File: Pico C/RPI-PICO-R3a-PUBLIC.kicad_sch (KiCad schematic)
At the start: 37 parts, among them IC1 W25Q16JVUXIQ, J1 CON_PICO_40W_VER_C, J2 USB_C_Receptacle_USB2.0_16P, J3 SM03B-SRSS-TB, Q1 DMG1012T-7, U2 RT6150B-33GQW, Y1 ECS-120-8-33-JGN-TR

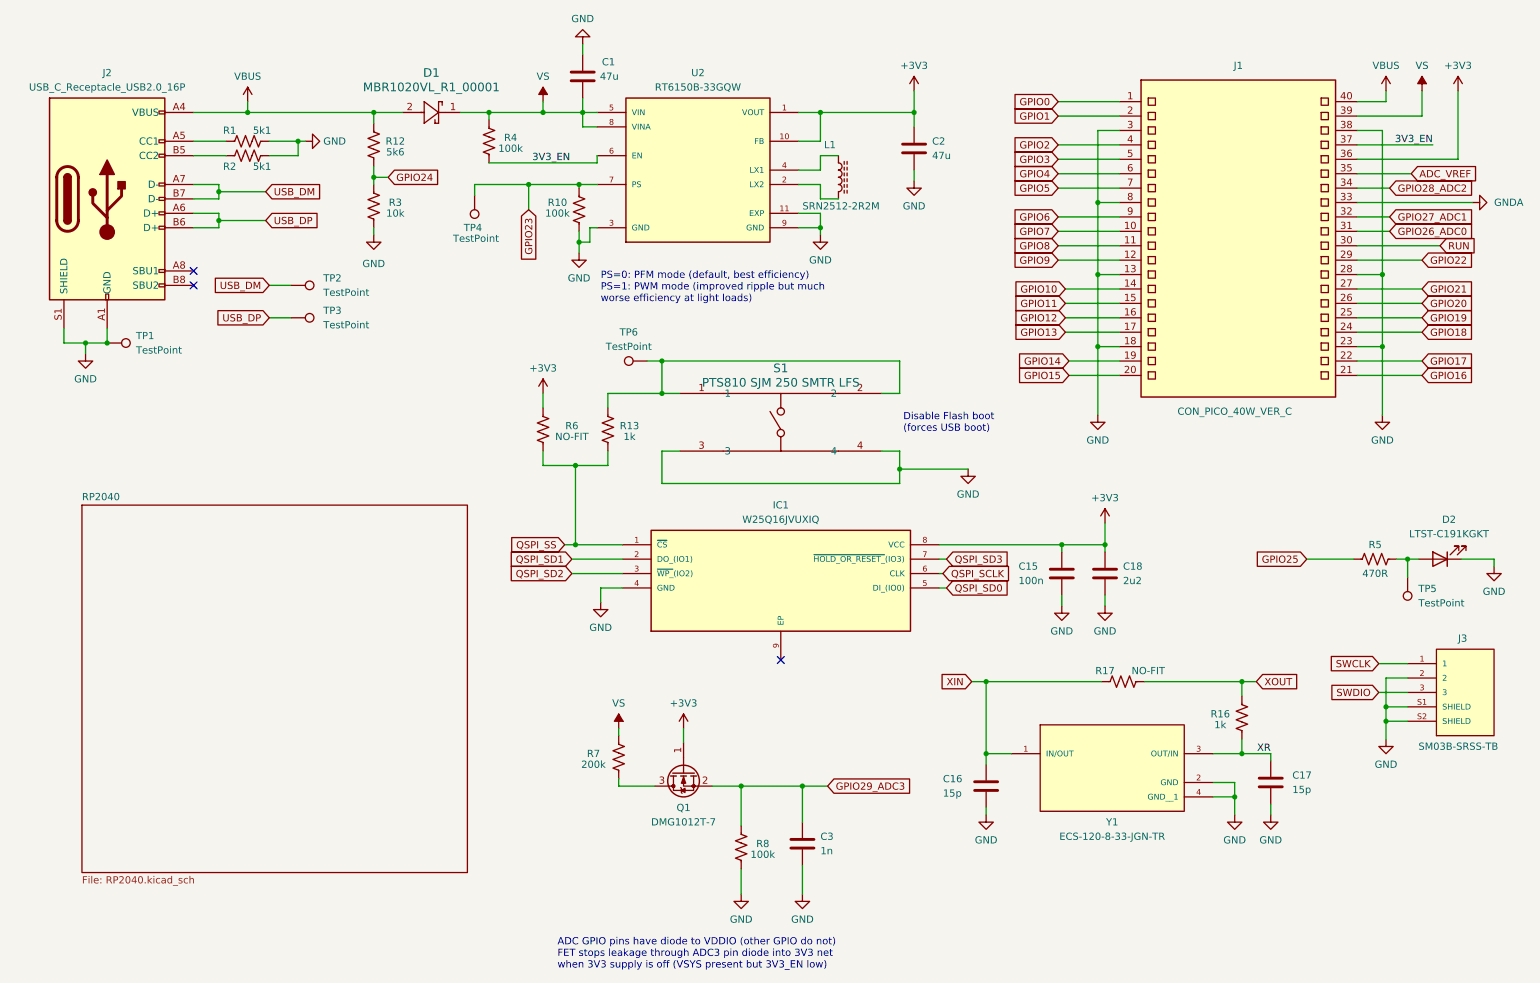
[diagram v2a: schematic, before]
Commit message: Add files via upload
Updated design and included official design file from the Pi Foundation.
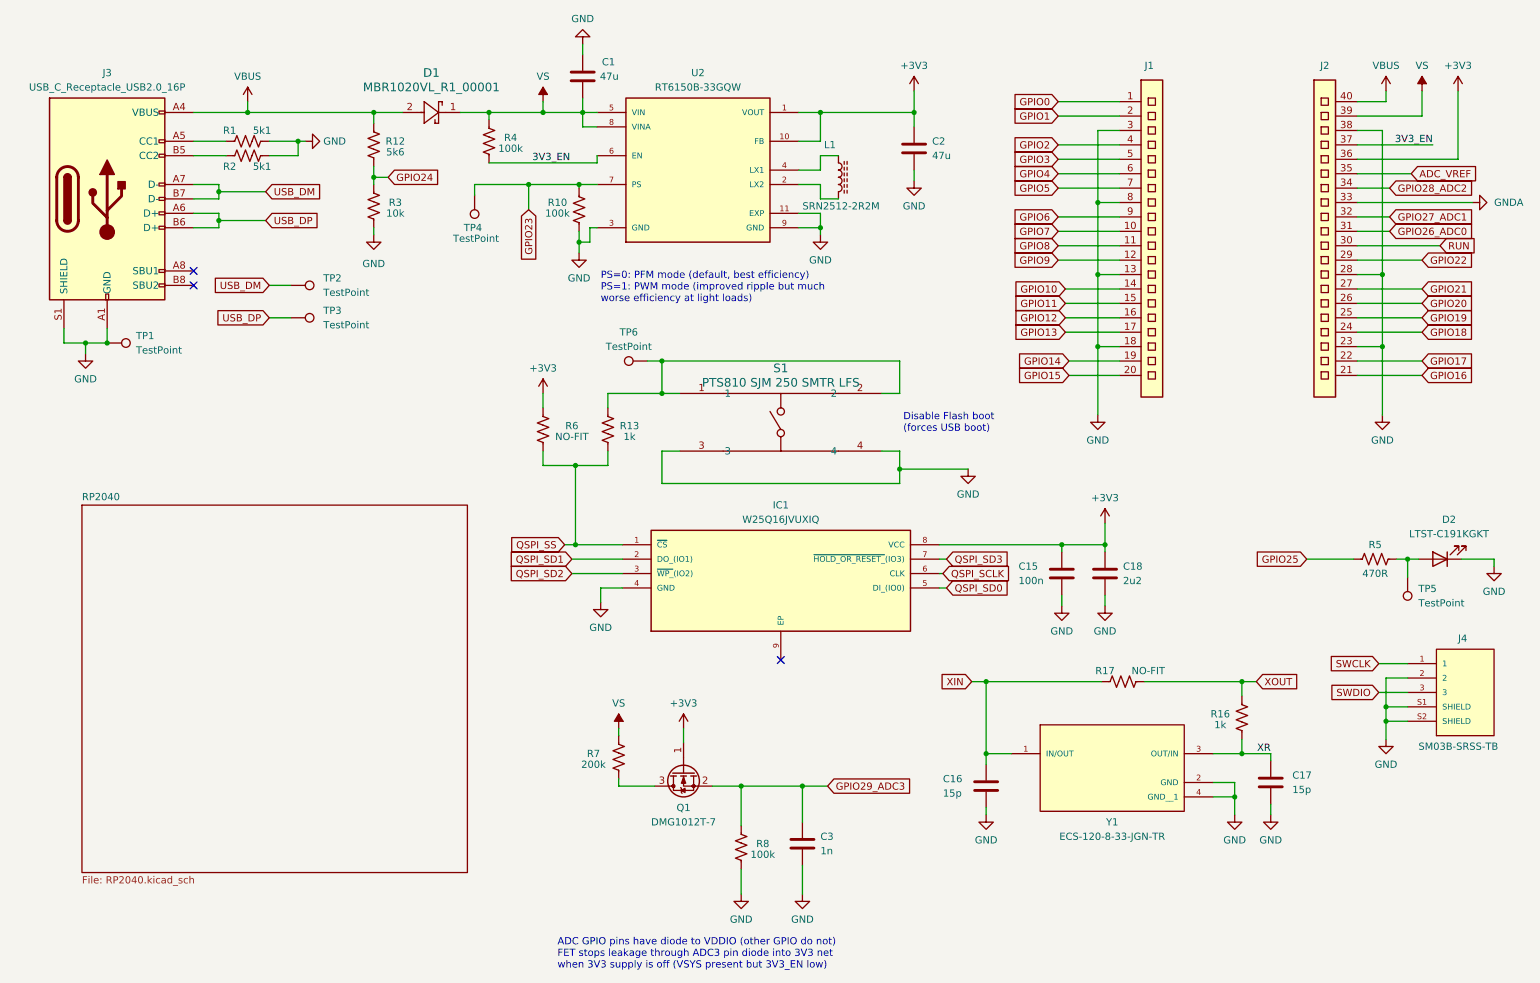
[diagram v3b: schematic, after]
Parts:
- removed J1: CON_PICO_40W_VER_C, Pico_C:CON_PICO_40W_VER_C, symbol Pico_C:CON_PICO_40W_VER_C
- removed J2: USB_C_Receptacle_USB2.0_16P, Connector_USB:USB_C_Receptacle_GCT_USB4105-xx-A_16P_TopMnt_Horizontal, symbol Connector:USB_C_Receptacle_USB2.0_16P
- removed J3: SM03B-SRSS-TB, Pico_C:JST_SM03B-SRSS-TB_LF__SN_, symbol Pico_C:SM03B-SRSS-TB_LF__SN_
- added J1: ~, Pico_C:CON_PICO_1-20, symbol Pico_C:CON_PICO_1-20
- added J2: ~, Pico_C:CON_PICO_21-40, symbol Pico_C:CON_PICO_21-40
- added J3: USB_C_Receptacle_USB2.0_16P, Connector_USB:USB_C_Receptacle_GCT_USB4105-xx-A_16P_TopMnt_Horizontal, symbol Connector:USB_C_Receptacle_USB2.0_16P
- added J4: SM03B-SRSS-TB, Pico_C:JST_SM03B-SRSS-TB_LF__SN_, symbol Pico_C:SM03B-SRSS-TB_LF__SN_
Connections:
- net +3V3: now also J2.36
- net 3V3_EN: now also J2.37
- net ADC_VREF: now also J2.35
- net GND: now also J1.13, J1.18, J1.3, J1.8, J2.23, J2.28, J2.38, J3.A1 (GND), J3.A12 (GND), J3.B1 (GND), J3.B12 (GND), J3.S1 (SHIELD), J4.2, J4.S1 (SHIELD), J4.S2 (SHIELD)
- net GNDA: now also J2.33
- net GPIO0: now also J1.1
- net GPIO1: now also J1.2
- net GPIO10: now also J1.14
- net GPIO11: now also J1.15
- net GPIO12: now also J1.16
- net GPIO13: now also J1.17
- net GPIO14: now also J1.19
- net GPIO15: now also J1.20
- net GPIO16: now also J2.21
- net GPIO17: now also J2.22
- net GPIO18: now also J2.24
- net GPIO19: now also J2.25
- net GPIO2: now also J1.4
- net GPIO20: now also J2.26
- net GPIO21: now also J2.27
- net GPIO22: now also J2.29
- net GPIO26_ADC0: now also J2.31
- net GPIO27_ADC1: now also J2.32
- net GPIO28_ADC2: now also J2.34
- net GPIO3: now also J1.5
- net GPIO4: now also J1.6
- net GPIO5: now also J1.7
- net GPIO6: now also J1.9
- net GPIO7: now also J1.10
- net GPIO8: now also J1.11
- net GPIO9: now also J1.12
- net RUN: now also J2.30
- net SWCLK: now also J4.1
- net SWDIO: now also J4.3
- net USB_DM: now also J3.A7 (D-), J3.B7 (D-)
- net USB_DP: now also J3.A6 (D+), J3.B6 (D+)
- net VBUS: now also J2.40, J3.A4 (VBUS), J3.A9 (VBUS), J3.B4 (VBUS), J3.B9 (VBUS)
- net VS: now also J2.39
- net at R1.1: now also J3.A5 (CC1)
- net at R2.1: now also J3.B5 (CC2)
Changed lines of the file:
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@@
-    )
-  )
-  (symbol (lib_id "Pico_C:SM03B-SRSS-TB_LF__SN_") (at 269.875 135.89 0) (unit 1)
-    (in_bom yes) (on_board yes) (dnp no)
-    (property "Reference" "J3" (at 268.605 126.365 0)
-      (effects (font (size 1.27 1.27)) (justify left))
-    )
-    (property "Value" "SM03B-SRSS-TB" (at 261.62 145.415 0)
-      (effects (font (size 1.27 1.27)) (justify left))
-    )
-    (property "Footprint" "Pico_C:JST_SM03B-SRSS-TB_LF__SN_" (at 269.875 135.89 0)
-      (effects (font (size 1.27 1.27)) (justify bottom) hide)
-    )
-    (property "Datasheet" "https://www.jst-mfg.com/product/pdf/eng/eSH.pdf" (at 269.875 135.89 0)
-      (effects (font (size 1.27 1.27)) hide)
-    )
-    (pin "2")
-    (pin "3")
-    (pin "S2")
-    (pin "1")
-    (pin "S1")
-    (instances
-      (project "RPI-PICO-R3a-PUBLIC"
-        (path "/f8a1033e-7d4e-4018-9b4c-1da5b150b31c"
-          (reference "J3") (unit 1)
-        )
-      )
     )
   )
@@
     )
   )
+  (symbol (lib_id "Connector:USB_C_Receptacle_USB2.0_16P") (at 30.48 48.895 0) (unit 1)
+    (in_bom yes) (on_board yes) (dnp no)
+    (property "Reference" "J3" (at 30.48 26.67 0)
+      (effects (font (size 1.27 1.27)))
+    )
+    (property "Value" "USB_C_Receptacle_USB2.0_16P" (at 30.48 29.21 0)
+      (effects (font (size 1.27 1.27)))
+    )
+    (property "Footprint" "Connector_USB:USB_C_Receptacle_GCT_USB4105-xx-A_16P_TopMnt_Horizontal" (at 34.29 48.895 0)
+      (effects (font (size 1.27 1.27)) hide)
+    )
+    (property "Datasheet" "https://www.usb.org/sites/default/files/documents/usb_type-c.zip" (at 34.29 48.895 0)
+      (effects (font (size 1.27 1.27)) hide)
+    )
+    (pin "S1")
+    (pin "A7")
+    (pin "B1")
+    (pin "B6")
+    (pin "B7")
+    (pin "A4")
+    (pin "A9")
+    (pin "A1")
+    (pin "B4")
+    (pin "B5")
+    (pin "A8")
+    (pin "A12")
+    (pin "A5")
+    (pin "B8")
+    (pin "A6")
+    (pin "B12")
+    (pin "B9")
+    (instances
+      (project "RPI-PICO-R3a-PUBLIC"
+        (path "/f8a1033e-7d4e-4018-9b4c-1da5b150b31c"
+          (reference "J3") (unit 1)
+        )
+      )
+    )
+  )
   (symbol (lib_id "Pico_C:ECS-120-8-33-JGN-TR") (at 207.645 149.225 0) (unit 1)
     (in_bom yes) (on_board yes) (dnp no)
@@
     )
   )
-  (symbol (lib_id "Pico_C:CON_PICO_40W_VER_C") (at 229.235 54.61 0) (unit 1)
-    (in_bom yes) (on_board yes) (dnp no)
-    (property "Reference" "J1" (at 229.87 25.4 0)
-      (effects (font (size 1.27 1.27)))
-    )
-    (property "Value" "CON_PICO_40W_VER_C" (at 229.235 86.36 0)
-      (effects (font (size 1.27 1.27)))
-    )
-    (property "Footprint" "Pico_C:CON_PICO_40W_VER_C" (at 230.505 69.85 0)
+  (symbol (lib_id "Device:C") (at 206.375 114.935 0) (unit 1)
+    (in_bom yes) (on_board yes) (dnp no) (fields_autoplaced)
+    (property "Reference" "C18" (at 209.55 113.665 0)
+      (effects (font (size 1.27 1.27)) (justify left))
+    )
+    (property "Value" "2u2" (at 209.55 116.205 0)
+      (effects (font (size 1.27 1.27)) (justify left))
+    )
+    (property "Footprint" "Capacitor_SMD:C_0402_1005Metric" (at 207.3402 118.745 0)
+      (effects (font (size 1.27 1.27)) hide)
+    )
+    (property "Datasheet" "~" (at 206.375 114.935 0)
+      (effects (font (size 1.27 1.27)) hide)
+    )
+    (pin "1")
+    (pin "2")
+    (instances
+      (project "RPI-PICO-R3a-PUBLIC"
+        (path "/f8a1033e-7d4e-4018-9b4c-1da5b150b31c"
+          (reference "C18") (unit 1)
+        )
+      )
+    )
+  )
+  (symbol (lib_id "Pico_C:CON_PICO_1-20") (at 229.235 54.61 0) (unit 1)
+    (in_bom yes) (on_board yes) (dnp no)
+    (property "Reference" "J1" (at 213.36 25.4 0)
+      (effects (font (size 1.27 1.27)) (justify left))
+    )
+    (property "Value" "~" (at 233.045 69.85 0)
+      (effects (font (size 1.27 1.27)))
+    )
+    (property "Footprint" "Pico_C:CON_PICO_1-20" (at 230.505 69.85 0)
       (effects (font (size 1.27 1.27)) hide)
     )
@@
       (effects (font (size 1.27 1.27)) hide)
     )
-    (pin "33")
+    (pin "20")
+    (pin "7")
+    (pin "11")
+    (pin "18")
+    (pin "2")
+    (pin "5")
+    (pin "9")
+    (pin "13")
+    (pin "4")
+    (pin "14")
+    (pin "16")
+    (pin "19")
+    (pin "15")
     (pin "10")
-    (pin "34")
-    (pin "27")
-    (pin "28")
-    (pin "15")
-    (pin "32")
-    (pin "16")
-    (pin "25")
+    (pin "6")
+    (pin "17")
     (pin "8")
-    (pin "29")
-    (pin "18")
-    (pin "2")
-    (pin "40")
-    (pin "35")
-    (pin "21")
-    (pin "22")
-    (pin "38")
-    (pin "9")
-    (pin "23")
-    (pin "11")
+    (pin "1")
     (pin "12")
-    (pin "13")
-    (pin "17")
-    (pin "31")
     (pin "3")
-    (pin "14")
-    (pin "36")
-    (pin "5")
-    (pin "7")
-    (pin "39")
-    (pin "24")
-    (pin "19")
-    (pin "37")
-    (pin "4")
-    (pin "6")
-    (pin "20")
-    (pin "26")
-    (pin "1")
-    (pin "30")
     (instances
       (project "RPI-PICO-R3a-PUBLIC"
         (path "/f8a1033e-7d4e-4018-9b4c-1da5b150b31c"
           (reference "J1") (unit 1)
-        )
-      )
-    )
-  )
-  (symbol (lib_id "Device:C") (at 206.375 114.935 0) (unit 1)
-    (in_bom yes) (on_board yes) (dnp no) (fields_autoplaced)
-    (property "Reference" "C18" (at 209.55 113.665 0)
-      (effects (font (size 1.27 1.27)) (justify left))
-    )
-    (property "Value" "2u2" (at 209.55 116.205 0)
-      (effects (font (size 1.27 1.27)) (justify left))
-    )
-    (property "Footprint" "Capacitor_SMD:C_0402_1005Metric" (at 207.3402 118.745 0)
-      (effects (font (size 1.27 1.27)) hide)
-    )
-    (property "Datasheet" "~" (at 206.375 114.935 0)
-      (effects (font (size 1.27 1.27)) hide)
-    )
-    (pin "1")
-    (pin "2")
-    (instances
-      (project "RPI-PICO-R3a-PUBLIC"
-        (path "/f8a1033e-7d4e-4018-9b4c-1da5b150b31c"
-          (reference "C18") (unit 1)
         )
       )
@@
     )
   )
+  (symbol (lib_id "Pico_C:SM03B-SRSS-TB_LF__SN_") (at 269.875 135.89 0) (unit 1)
+    (in_bom yes) (on_board yes) (dnp no)
+    (property "Reference" "J4" (at 268.605 126.365 0)
+      (effects (font (size 1.27 1.27)) (justify left))
+    )
+    (property "Value" "SM03B-SRSS-TB" (at 261.62 145.415 0)
+      (effects (font (size 1.27 1.27)) (justify left))
+    )
+    (property "Footprint" "Pico_C:JST_SM03B-SRSS-TB_LF__SN_" (at 269.875 135.89 0)
+      (effects (font (size 1.27 1.27)) (justify bottom) hide)
+    )
+    (property "Datasheet" "https://www.jst-mfg.com/product/pdf/eng/eSH.pdf" (at 269.875 135.89 0)
+      (effects (font (size 1.27 1.27)) hide)
+    )
+    (pin "2")
+    (pin "S1")
+    (pin "3")
+    (pin "1")
+    (pin "S2")
+    (instances
+      (project "RPI-PICO-R3a-PUBLIC"
+        (path "/f8a1033e-7d4e-4018-9b4c-1da5b150b31c"
+          (reference "J4") (unit 1)
+        )
+      )
+    )
+  )
   (symbol (lib_id "power:GND") (at 185.42 157.48 0) (unit 1)
     (in_bom yes) (on_board yes) (dnp no) (fields_autoplaced)
@@
     )
   )
-  (symbol (lib_id "Connector:USB_C_Receptacle_USB2.0_16P") (at 30.48 48.895 0) (unit 1)
-    (in_bom yes) (on_board yes) (dnp no) (fields_autoplaced)
-    (property "Reference" "J2" (at 30.48 26.67 0)
-      (effects (font (size 1.27 1.27)))
-    )
-    (property "Value" "USB_C_Receptacle_USB2.0_16P" (at 30.48 29.21 0)
-      (effects (font (size 1.27 1.27)))
-    )
-    (property "Footprint" "Connector_USB:USB_C_Receptacle_GCT_USB4105-xx-A_16P_TopMnt_Horizontal" (at 34.29 48.895 0)
-      (effects (font (size 1.27 1.27)) hide)
-    )
-    (property "Datasheet" "https://www.usb.org/sites/default/files/documents/usb_type-c.zip" (at 34.29 48.895 0)
-      (effects (font (size 1.27 1.27)) hide)
-    )
-    (pin "A7")
-    (pin "A1")
-    (pin "A5")
-    (pin "A4")
-    (pin "B7")
-    (pin "B8")
-    (pin "A6")
-    (pin "A12")
-    (pin "B12")
-    (pin "B5")
-    (pin "B1")
-    (pin "B9")
-    (pin "S1")
-    (pin "A8")
-    (pin "B4")
-    (pin "A9")
-    (pin "B6")
-    (instances
-      (project "RPI-PICO-R3a-PUBLIC"
+  (symbol (lib_id "Pico_C:CON_PICO_21-40") (at 229.235 54.61 0) (unit 1)
+    (in_bom yes) (on_board yes) (dnp no) (fields_autoplaced)
+    (property "Reference" "J2" (at 245.11 25.4 0)
+      (effects (font (size 1.27 1.27)))
+    )
+    (property "Value" "~" (at 233.045 69.85 0)
+      (effects (font (size 1.27 1.27)))
+    )
+    (property "Footprint" "Pico_C:CON_PICO_21-40" (at 230.505 69.85 0)
+      (effects (font (size 1.27 1.27)) hide)
+    )
+    (property "Datasheet" "" (at 233.045 69.85 0)
+      (effects (font (size 1.27 1.27)) hide)
+    )
+    (pin "39")
+    (pin "30")
+    (pin "33")
+    (pin "27")
+    (pin "24")
+    (pin "22")
+    (pin "21")
+    (pin "23")
+    (pin "28")
+    (pin "36")
+    (pin "38")
+    (pin "35")
+    (pin "29")
+    (pin "40")
+    (pin "26")
+    (pin "25")
+    (pin "34")
+    (pin "32")
+    (pin "37")
+    (pin "31")
+    (instances
+      (project "RPI-PICO-R3a-PUBLIC"

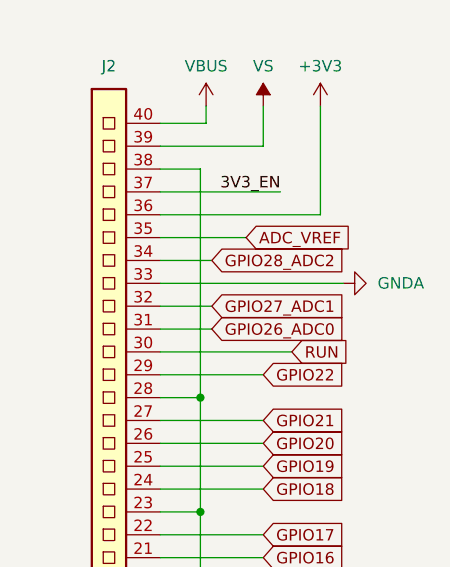
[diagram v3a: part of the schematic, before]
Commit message: Add files via upload
Corrected pin 33 to actually be GND instead of a NC to GNDA.
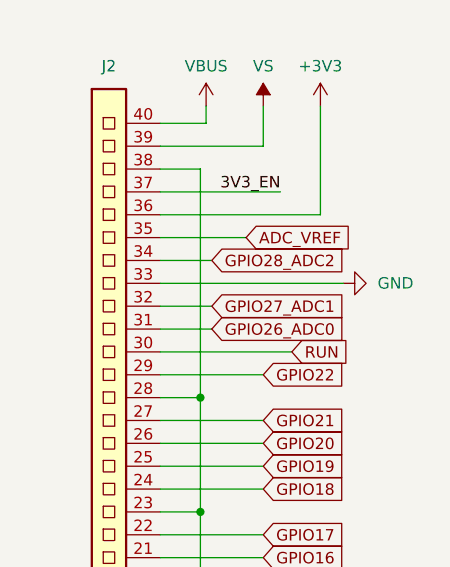
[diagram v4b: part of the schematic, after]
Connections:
- net GNDA is gone; now on net GND: J2.33
